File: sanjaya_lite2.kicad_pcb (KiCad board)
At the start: 2 copper layers, 110 parts, among them J1 12V_Out, J10 Adap_In, J11 DCDC_Bypass, J12 Conn_RS485, J13 Bat_Bypass+, J14 J_Bat, J15 Conn_420_1, J16 Conn_420_2, J17 Conn_420_3, J18 Conn_420_4, J19 Volt_check_5V, J2 J_SW_Esp, J20 Pwr_SW, J21 J_SW_Sim800, J22 UART_Sim800, J23 Bat_Prot_Bypass, J24 Bat_Bypass-, J3 5V_Out, J4 J_LED, J5 VBat_Out, J6 Conn_I2C, J7 Conn_SPI, J8 Conn_I2C, J9 J_UART_DBG, Q1 PMOS_SI2369DS, Q2 BSS138, Q3 BSS138, SW1 SW_Reset, SW2 SW_Boot, U1 ESP32-WROOM-32, U2 MCP1700-3302E_SOT23, U3 SN65HVD75DR, U5 MCP3428

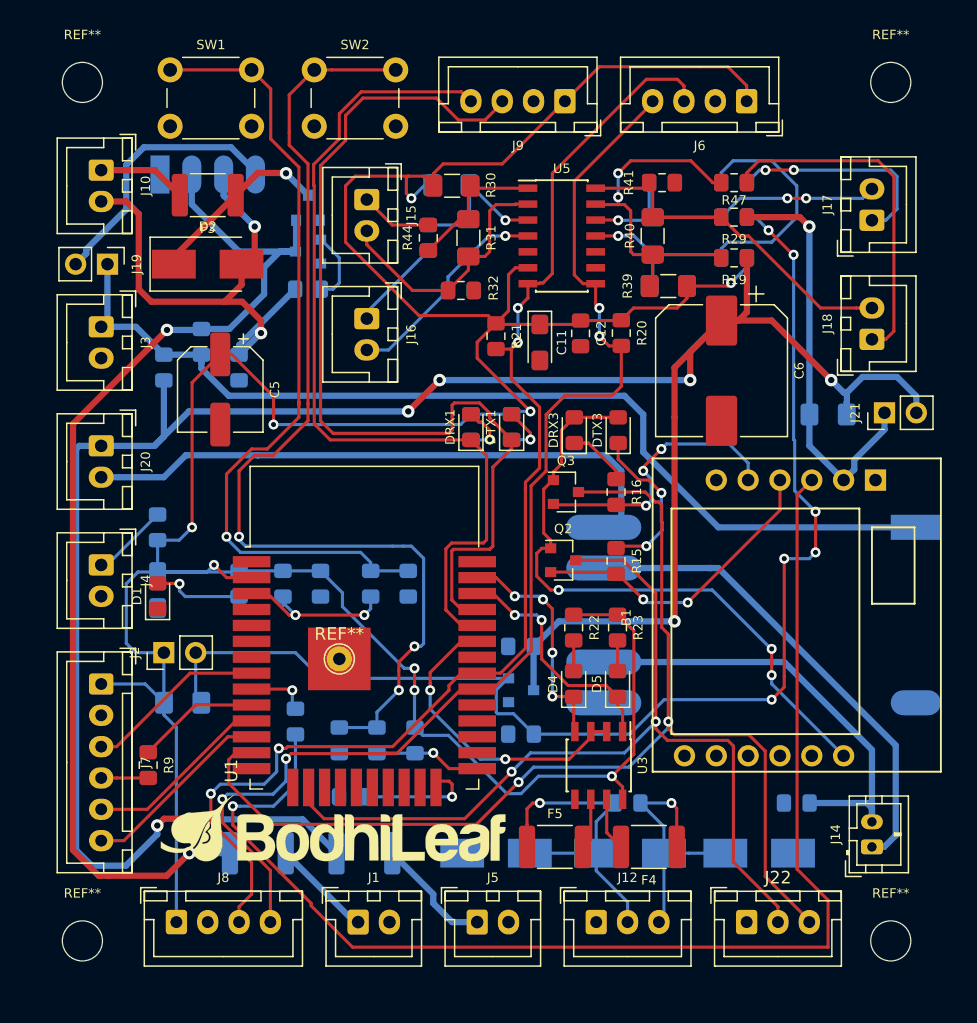
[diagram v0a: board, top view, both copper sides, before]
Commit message: Ground pour on F.Cu and B.Cu added. DRC still not passing. Checking in to save work
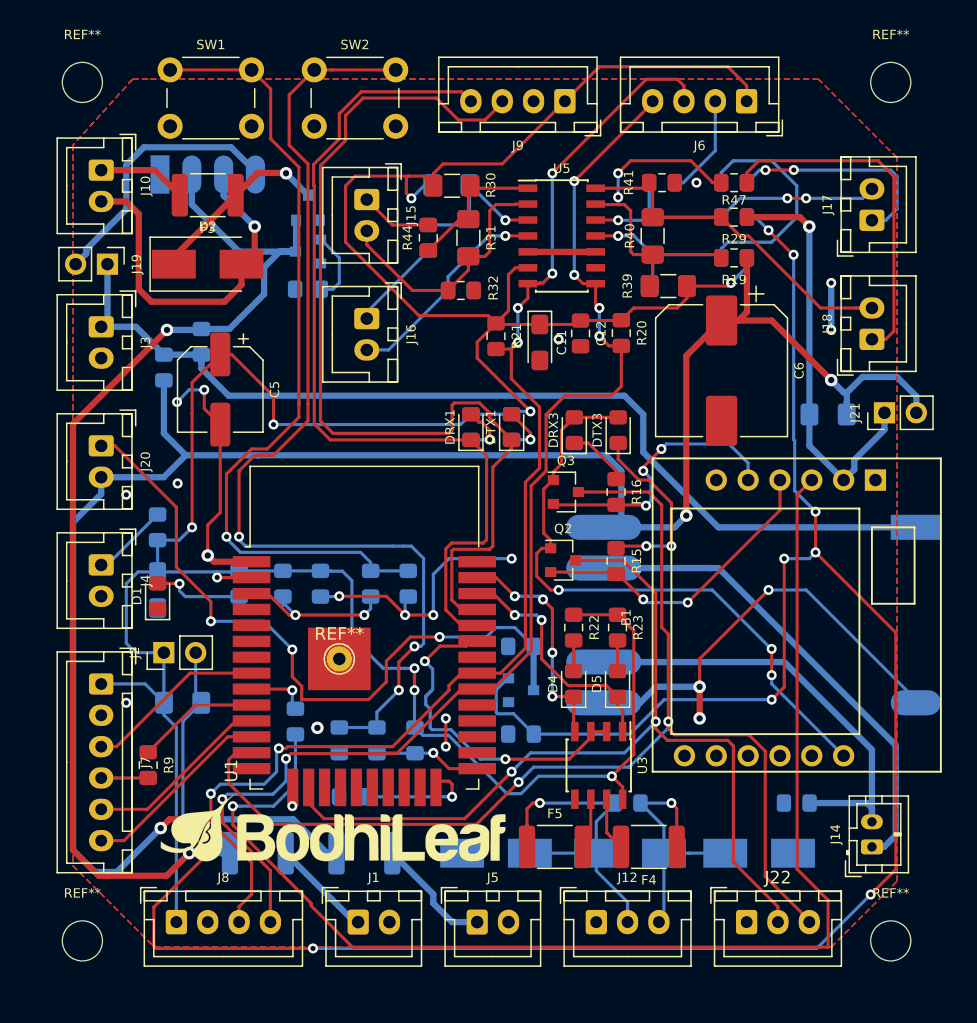
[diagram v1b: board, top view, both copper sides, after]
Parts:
- removed J24: Bat_Bypass-, Resistor_SMD:R_0805_2012Metric_Pad1.15x1.40mm_HandSolder
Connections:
- B2 pad 3: Net-(B2-Pad3) -> /GND_Supply
- B3 pad 2: Net-(B2-Pad3) -> /GND_Supply
- B3 pad 6: Net-(B3-Pad6) -> /Sim800_I_Sense+
- C7 pad 1: /Sim800_I_Sense+ -> Net-(C7-Pad1)
- D2 pad 2: Net-(B2-Pad3) -> /GND_Supply
- J10 pad 2: Net-(B2-Pad3) -> /GND_Supply
- J20 pad 1: /Sim800_I_Sense+ -> Net-(C7-Pad1)
- J20 pad 2: Net-(B3-Pad6) -> /Sim800_I_Sense+
- R14 pad 2: Net-(B2-Pad3) -> /GND_Supply
- U2 pad 3: /Sim800_I_Sense+ -> Net-(C7-Pad1)
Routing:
- net /GND_Supply: track 0.00 -> 124.6 mm, vias 0 -> 22
- net /Esp_I_Sense-: track 100.8 -> 187.1 mm, vias 6 -> 9
- net Net-(C7-Pad1): track 0.00 -> 56.0 mm, vias 0 -> 3
- net Net-(B3-Pad6): track 47.2 -> 0.00 mm
- net Net-(B2-Pad3): track 42.2 -> 0.00 mm, vias 2 -> 0
- net /Sim800_I_Sense+: track 188.9 -> 160.3 mm, vias 7 -> 4
- net /rs485/DE: track 24.1 -> 27.9 mm
- net /Esp_I_Sense+: track 264.9 -> 262.0 mm
- net Net-(DTX3-Pad1): track 13.1 -> 14.9 mm
- net /SDA: vias 4 -> 6
- net /SCL: vias 4 -> 6
- added copper zone on B.Cu, net /GND_Supply
- added copper zone on F.Cu, net /GND_Supply

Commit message: No unconnected tracks. DRC not passing due to one minor issue: ESP pad 39 and solder pad behind it not connected. This is because pad 39 doesn't show up in the schematic and the solder pad behind it is added directly in pcbnew and hence there is no net connecting them
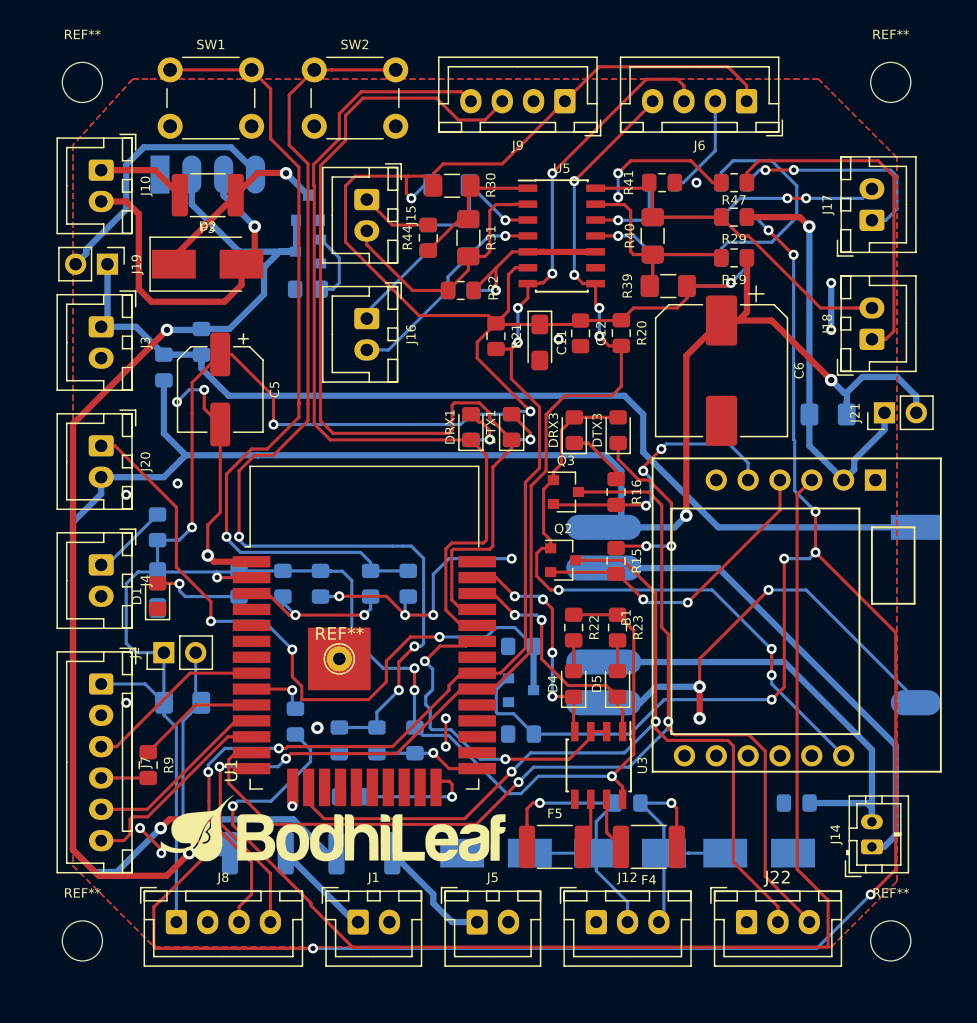
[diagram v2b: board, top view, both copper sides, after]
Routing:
- net /GND_Supply: track 124.6 -> 136.5 mm, vias 22 -> 25
- net /Esp_I_Sense+: track 262.0 -> 265.6 mm
- net /SCL: track 103.1 -> 104.0 mm
- net /SDA: track 96.3 -> 97.1 mm
- net /MOSI_RLY2: track 15.9 -> 16.6 mm
- net /Sim800_RST: track 101.6 -> 102.3 mm

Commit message: DRC passing after ESP footprint was edited for the thermal pad. Edge cut layer added
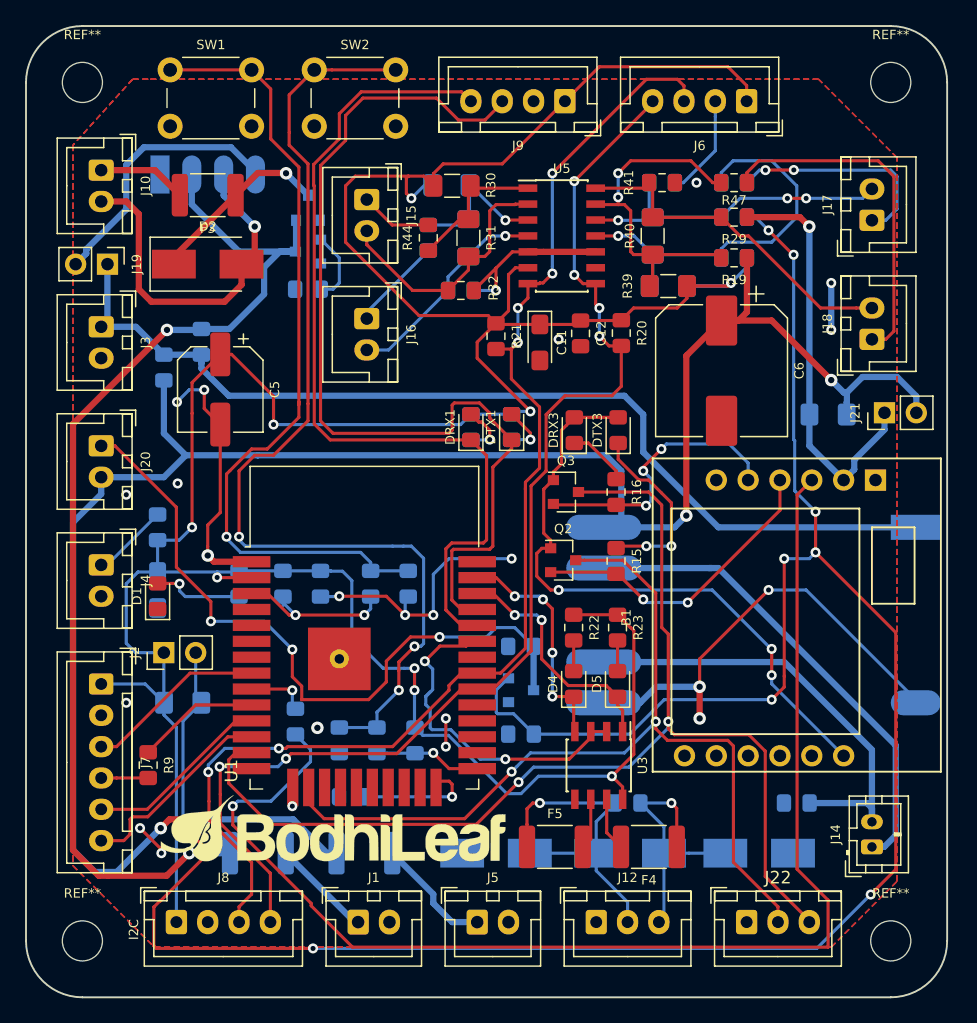
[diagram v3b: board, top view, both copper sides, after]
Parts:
- removed the REF** at (110.5, 106.0)
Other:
- board outline added: 73.5 x 77.5 mm
- board text added: "I2C"

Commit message: 1. Corrected a schematics error where power switch was not cutting power off to VBAT. Made corresponding changes to pcb layout and routing 2. LDO physical location was causing problems with new routing and ground plane stitching. Moved it from right of ESP to its left. 3. DRC is fully passing. 4. Some informative text added
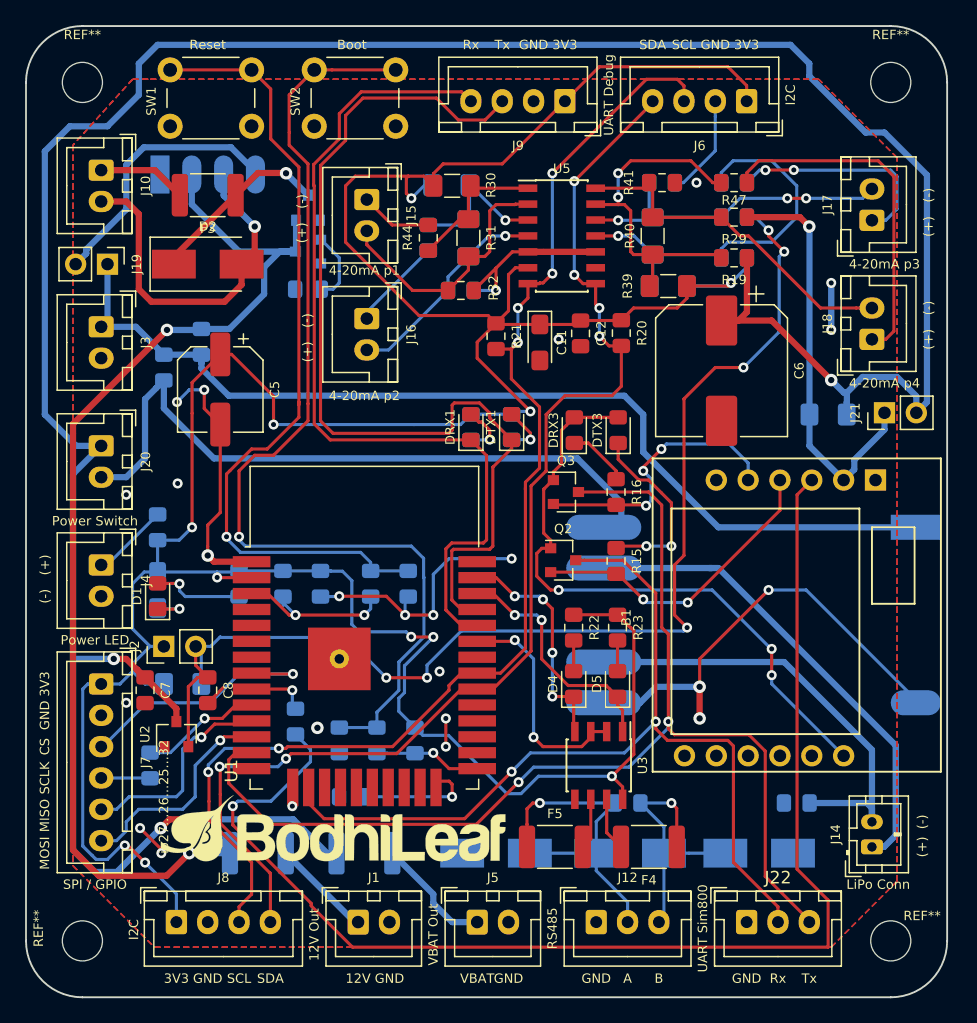
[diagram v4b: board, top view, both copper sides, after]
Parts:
- C7, C8, U2: moved to F.Cu
- R9: moved to B.Cu
- moved C7 30.2 mm to (95.0, 108.5), turned to 270 degrees
- moved U2 27.7 mm to (97.5, 112.0), turned to 90 degrees
- moved C8 25.2 mm to (100.0, 108.5), turned to 270 degrees
- moved R7 1.50 mm to (98.0, 108.0)
- moved J2 0.50 mm to (96.5, 105.0)
- moved R9 0.15 mm to (95.4, 114.5)
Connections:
- B3 pad 6: /Sim800_I_Sense+ -> Net-(B3-Pad6)
- C7 pad 1: Net-(C7-Pad1) -> /Sim800_I_Sense+
- J13 pad 1: /Sim800_I_Sense+ -> Net-(B3-Pad6)
- J20 pad 1: Net-(C7-Pad1) -> /Sim800_I_Sense+
- J20 pad 2: /Sim800_I_Sense+ -> Net-(B3-Pad6)
- U2 pad 3: Net-(C7-Pad1) -> /Sim800_I_Sense+
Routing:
- net /Esp_I_Sense-: track 187.1 -> 95.8 mm, vias 9 -> 6
- net /Sim800_I_Sense+: track 160.3 -> 223.4 mm
- net Net-(C7-Pad1): track 56.0 -> 0.00 mm, vias 3 -> 0
- net Net-(B3-Pad6): track 0.00 -> 53.9 mm
- net /Esp_I_Sense+: track 265.6 -> 275.1 mm, vias 9 -> 11
- net /rs485/DE: track 27.9 -> 19.6 mm
- net /CS: track 14.9 -> 21.0 mm, vias 0 -> 1
- net /GND_Supply: track 136.5 -> 141.8 mm, vias 25 -> 27
- net /MISO_RLY1: track 15.4 -> 17.4 mm, vias 0 -> 1
- net /MOSI_RLY2: track 16.6 -> 17.8 mm, vias 0 -> 1
- net Net-(C4-Pad1): track 82.3 -> 82.0 mm, vias 3 -> 1
- net /SCLK: track 10.3 -> 10.2 mm, vias 0 -> 1
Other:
- board text added: "(+)"
- board text added: "(-)"
- board text added: "12V"
- board text added: "12V Out"
- board text added: "3V3"
- board text added: "4-20mA p1"
- board text added: "4-20mA p2"
- board text added: "4-20mA p3"
- board text added: "4-20mA p4"
- board text added: "A"
- board text added: "B"
- board text added: "Boot"
- board text added: "CS"
- board text added: "GND"
- board text added: "LiPo Conn"
- board text added: "MISO"
- board text added: "MOSI"
- board text added: "Power LED"
- board text added: "Power Switch"
- board text added: "RS485"
- board text added: "Reset"
- board text added: "Rx"
- board text added: "SCL"
- board text added: "SCLK"
- board text added: "SDA"
- board text added: "SPI / GPIO"
- board text added: "Tx"
- board text added: "UART Debug"
- board text added: "UART Sim800"
- board text added: "VBAT"
- board text added: "VBAT Out"
- board text added: "io27...26...25...32"

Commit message: Text added. J11 and J13 were found to be underneath dc-dc board footprint. Need to repair it
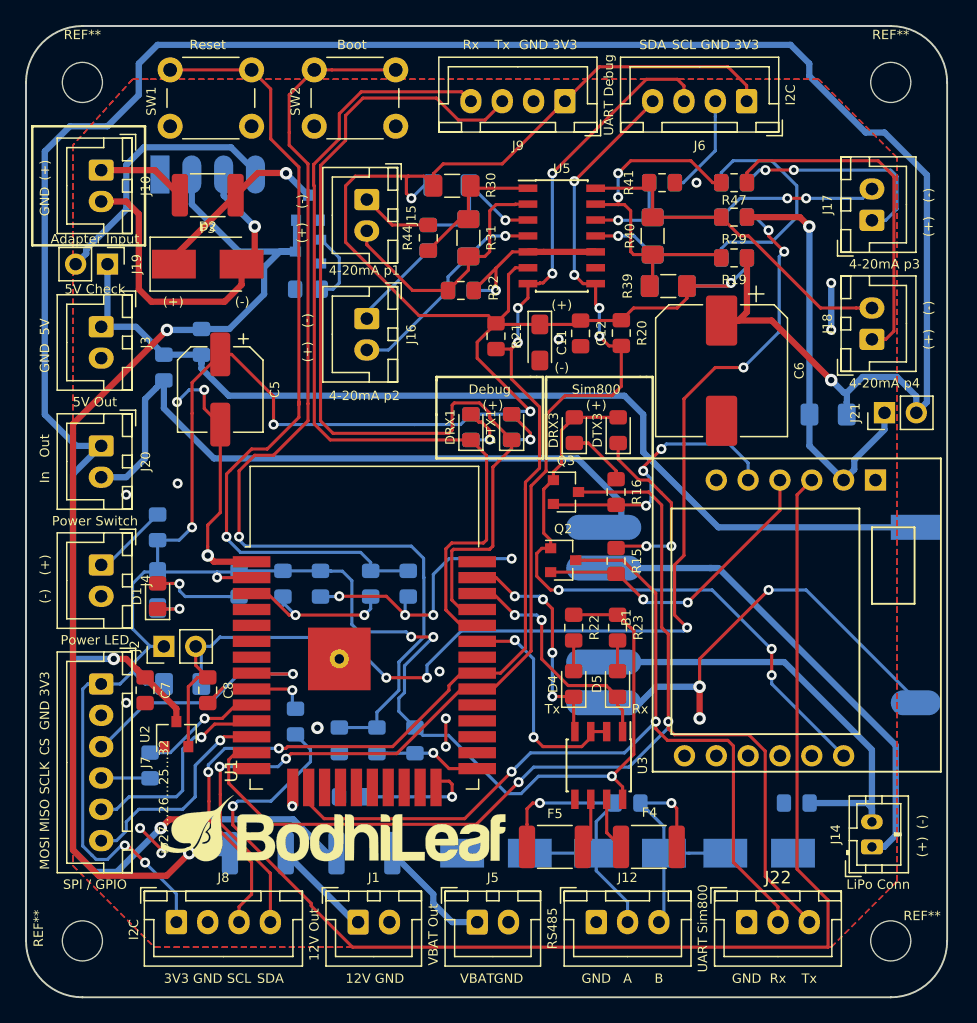
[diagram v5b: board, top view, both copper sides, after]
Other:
- board text added: "5V"
- board text added: "5V Check"
- board text added: "5V Out"
- board text added: "Adapter Input"
- board text added: "Debug"
- board text added: "In"
- board text added: "Out"
- board text added: "Sim800"

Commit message: Bat_Bypass jumper resistor moved out of DC-DC board's footprint. DC-DC bypass jumper resistor left where it was as it will be soldered only when the DC-DC board isn't present
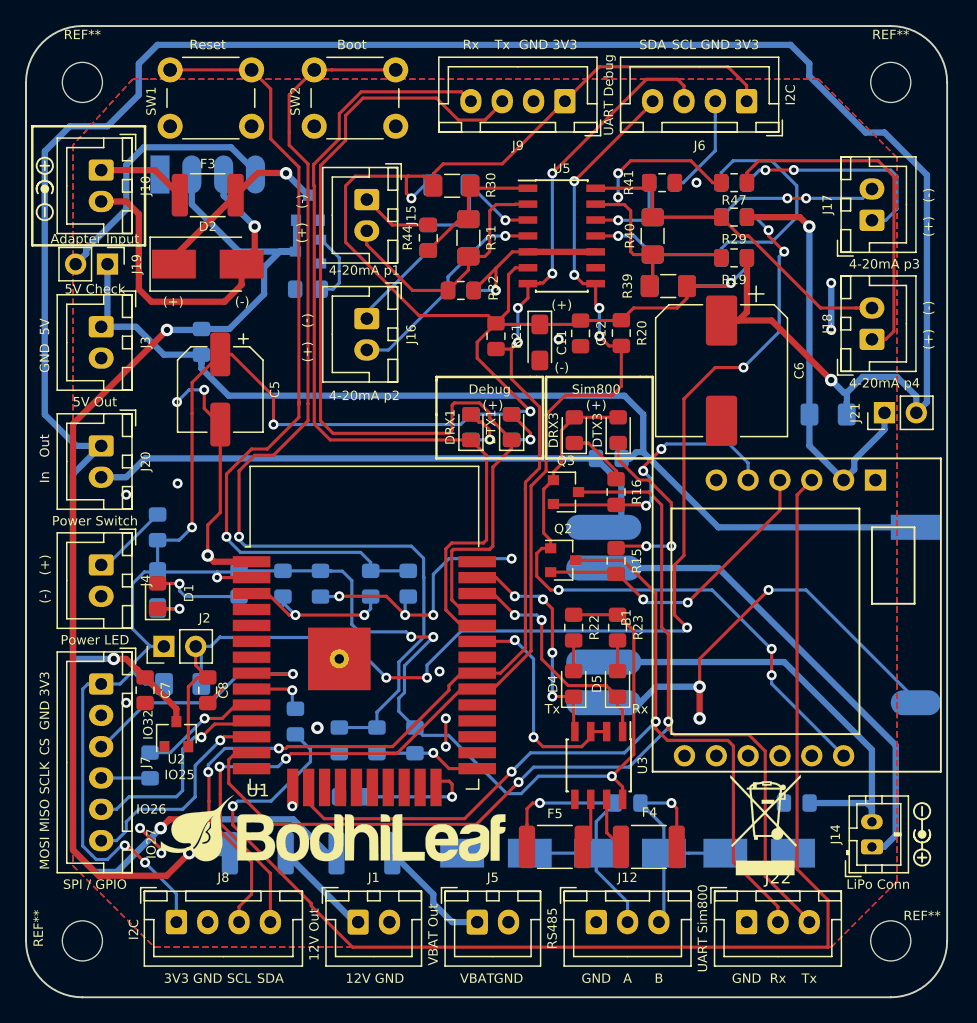
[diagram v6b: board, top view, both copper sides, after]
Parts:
- added G***: LOGO, Custom Silkscreens:Logo_silk_polarity_external_5x1.4mm, F.Cu at (87.0, 68.5)
- added G***: LOGO, Custom Silkscreens:Logo_silk_polarity_external_5x1.4mm, F.Cu at (157.0, 120.0)
- added G***: LOGO, Custom Silkscreens:logo, B.Cu at (138.5, 82.5)
- added REF**: WEEE-Logo_5.6x8mm_SilkScreen, Symbol:WEEE-Logo_5.6x8mm_SilkScreen, F.Cu at (144.5, 119.2)
- moved J13 36.2 mm to (132.0, 90.0), turned to 0 degrees
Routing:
- net Net-(B3-Pad6): track 53.9 -> 45.5 mm
- net /5V_Out: track 78.7 -> 80.7 mm
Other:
- board text added: "IO25"
- board text added: "IO26"
- board text added: "IO27"
- board text added: "IO32"
- board text removed: "io27...26...25...32"
